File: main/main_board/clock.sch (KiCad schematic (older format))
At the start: 12 parts, among them U10 74AUP1G74, U11 MCP1755S-3302E/DB, U12 FIN1047, X1 Si570

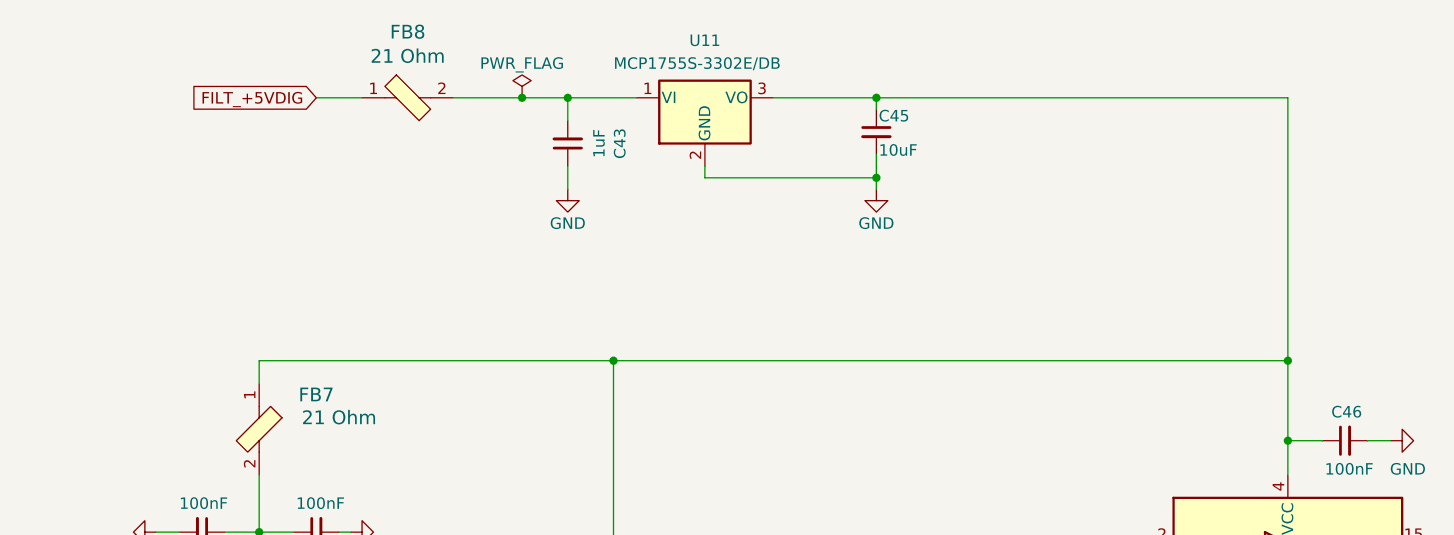
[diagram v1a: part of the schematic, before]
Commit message: A bunch of thinking about RFI and ESD, and some testing.  Mostly reflected in notebook.txt. Also another more explicit round of consideration of box-level grounding and power distribution, because this affects the power conditioning on the main board.  Power nets on the main board are mostly captured.  I added supply decoupling at each plugin slot.
in_filter.sxsch: added simulation of ESD, use vendor models for TVS diode and ferrite.

power_budget.xlsx: get rid of sheets for the input boards not implemented.  Add sheet for
the main board and carry over data from the input board sheet.
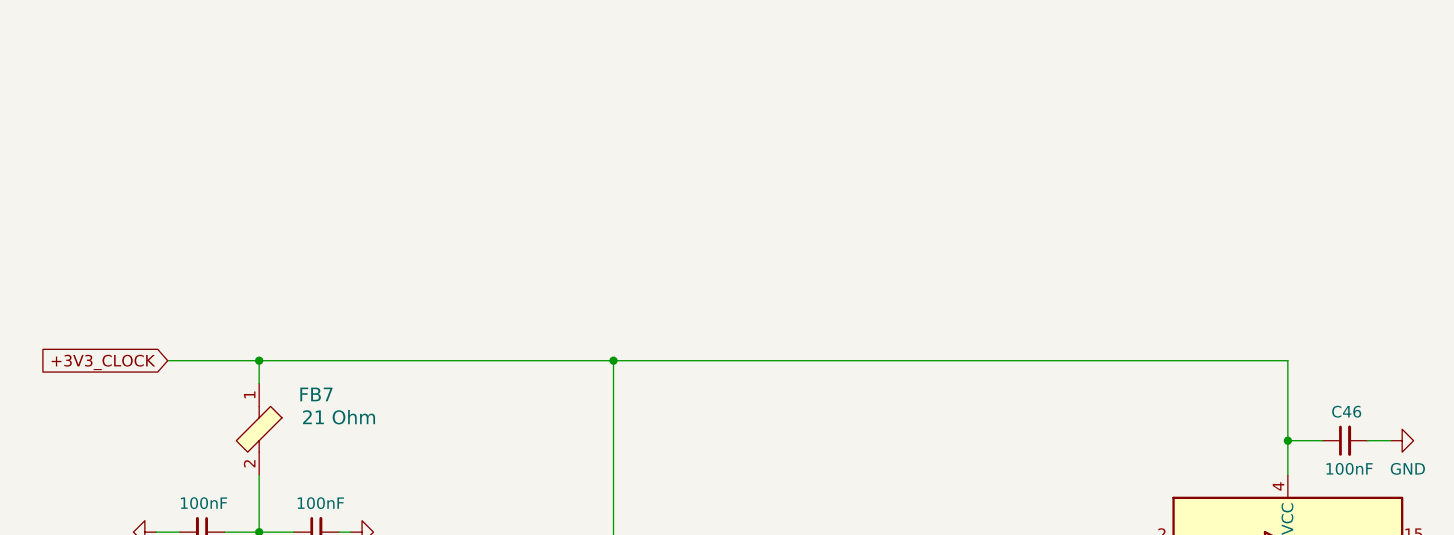
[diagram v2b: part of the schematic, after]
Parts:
- removed C43: 1uF, Capacitor_SMD:C_0805_2012Metric, symbol Device:C_Small
- removed C45: 10uF, Capacitor_SMD:C_0603_1608Metric, symbol Device:C_Small
- removed FB8: 21 Ohm, Inductor_SMD:L_0805_2012Metric, symbol dk_Ferrite-Beads-and-Chips:MPZ2012S601AT000
- removed U11: MCP1755S-3302E/DB, Package_TO_SOT_SMD:SOT-223-3_TabPin2, symbol Regulator_Linear:MCP1703A-1202_SOT223
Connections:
- net labels added: +3V3_CLOCK
- net labels removed: FILT_+5VDIG
- wire segments 64 -> 51
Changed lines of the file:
@@
 	4500 5100 4500 5250
 Connection ~ 4500 5250
-Text GLabel 3200 2150 0    50   Input ~ 0
-FILT_+5VDIG
-$Comp
-L Regulator_Linear:MCP1703A-1202_SOT223 U?
-U 1 1 5EC36C64
-P 4900 2150
-AR Path="/5E624B3C/5E51E83D/5EC36C64" Ref="U?"  Part="1"
-AR Path="/5E525F2C/5EC36C64" Ref="U11"  Part="1"
-F 0 "U11" H 4900 2400 50  0000 C CNN
-F 1 "MCP1755S-3302E/DB" H 4500 2300 50  0000 L CNN
-F 2 "Package_TO_SOT_SMD:SOT-223-3_TabPin2" H 4900 2350 50  0001 C CNN
-F 3 "http://www.microchip.com/mymicrochip/filehandler.aspx?ddocname=en560605" H 4900 2100 50  0001 C CNN
-F 4 "MCP1755S-3302E/DB-ND" H 4900 2150 50  0001 C CNN "Digikey"
-F 5 "IC REG LIN 3.3V 300MA SOT223-3" H 4900 2150 50  0001 C CNN "Description"
-F 6 "25" H 4900 2150 50  0001 C CNN "DK line"
-	1    4900 2150
-	1    0    0    -1
-$EndComp
-$Comp
-L dk_Ferrite-Beads-and-Chips:MPZ2012S601AT000 FB?
-U 1 1 5EC36C6F
-P 3600 2150
-AR Path="/5DFCF14D/5DE42731/5EC36C6F" Ref="FB?"  Part="1"
-AR Path="/5DFCF14D/5EC36C6F" Ref="FB?"  Part="1"
-AR Path="/5DFCF14D/5DA78AA2/5EC36C6F" Ref="FB?"  Part="1"
-AR Path="/5E51E83D/5EC36C6F" Ref="FB?"  Part="1"
-AR Path="/5E624B3C/5E51E83D/5EC36C6F" Ref="FB?"  Part="1"
-AR Path="/5E525F2C/5EC36C6F" Ref="FB8"  Part="1"
-F 0 "FB8" H 3600 2437 60  0000 C CNN
-F 1 "21 Ohm" H 3600 2331 60  0000 C CNN
-F 2 "Inductor_SMD:L_0805_2012Metric" H 3800 2350 60  0001 L CNN
-F 3 "https://www.yuden.co.jp/productdata/catalog/chipbeads01_e.pdf" H 3800 2450 60  0001 L CNN
-F 4 "HZ0805C202R-10" H 3800 2650 60  0001 L CNN "MPN"
-F 5 "Ferrite Beads and Chips" H 3800 2850 60  0001 L CNN "Family"
-F 6 "FERRITE BEAD 21 OHM 0805, 100 nH, 5 mOhm" H 3800 3150 60  0001 L CNN "Description"
-F 7 "587-1765-1-ND" H 3600 2150 50  0001 C CNN "Digikey"
-F 8 "24" H 3600 2150 50  0001 C CNN "DK line"
-	1    3600 2150
-	1    0    0    -1
-$EndComp
-$Comp
-L Device:C_Small C?
-U 1 1 5EC36C79
-P 4300 2350
-AR Path="/5DFF6C0D/5EC36C79" Ref="C?"  Part="1"
-AR Path="/5E1D6729/5E1DA2AA/5EC36C79" Ref="C?"  Part="1"
-AR Path="/5E2EB92B/5EC36C79" Ref="C?"  Part="1"
-AR Path="/5E51E83D/5EC36C79" Ref="C?"  Part="1"
-AR Path="/5E624B3C/5E51E83D/5EC36C79" Ref="C?"  Part="1"
-AR Path="/5E525F2C/5EC36C79" Ref="C43"  Part="1"
-F 0 "C43" V 4071 2350 50  0000 C CNN
-F 1 "1uF" V 4162 2350 50  0000 C CNN
-F 2 "Capacitor_SMD:C_0805_2012Metric" H 4300 2350 50  0001 C CNN
-F 3 "https://media.digikey.com/pdf/Data%20Sheets/Samsung%20PDFs/CL_Series_MLCC_ds.pdf" H 4300 2350 50  0001 C CNN
-F 4 "CAP CER 1UF 16V X7R 0805 " H 4300 2350 50  0001 C CNN "Description"
-F 5 "1276-6471-1-ND" H 4300 2350 50  0001 C CNN "Digikey"
-F 6 "CL21B105KOFNNNG" H 4300 2350 50  0001 C CNN "MPN"
-F 7 "27" H 4300 2350 50  0001 C CNN "DK line"
-	1    4300 2350
-	-1   0    0    1
-$EndComp
-Wire Wire Line
-	4300 2250 4300 2150
-Connection ~ 4300 2150
-Wire Wire Line
-	4300 2150 4600 2150
-Wire Wire Line
-	4300 2450 4300 2550
-Wire Wire Line
-	5650 2150 5650 2200
-Connection ~ 5650 2150
-Wire Wire Line
-	5650 2150 5200 2150
-Wire Wire Line
-	5650 2400 5650 2500
-Wire Wire Line
-	5650 2500 4900 2500
-Connection ~ 5650 2500
-Wire Wire Line
-	5650 2500 5650 2550
-Wire Wire Line
-	4900 2500 4900 2450
-Wire Wire Line
-	3200 2150 3400 2150
-$Comp
-L power:PWR_FLAG #FLG?
-U 1 1 5EC36CA7
-P 4100 2150
-AR Path="/5E624B3C/5E51E83D/5EC36CA7" Ref="#FLG?"  Part="1"
-AR Path="/5E525F2C/5EC36CA7" Ref="#FLG01"  Part="1"
-F 0 "#FLG01" H 4100 2225 50  0001 C CNN
-F 1 "PWR_FLAG" H 4100 2300 50  0000 C CNN
-F 2 "" H 4100 2150 50  0001 C CNN
-F 3 "~" H 4100 2150 50  0001 C CNN
-	1    4100 2150
-	1    0    0    -1
-$EndComp
-Connection ~ 4100 2150
-Wire Wire Line
-	4100 2150 4300 2150
-$Comp
-L power:GND #PWR?
-U 1 1 5EC36CB5
-P 5650 2550
-AR Path="/5E624B3C/5E51E83D/5EC36CB5" Ref="#PWR?"  Part="1"
-AR Path="/5E525F2C/5EC36CB5" Ref="#PWR051"  Part="1"
-F 0 "#PWR051" H 5650 2300 50  0001 C CNN
-F 1 "GND" H 5650 2400 50  0000 C CNN
-F 2 "" H 5650 2550 50  0001 C CNN
-F 3 "" H 5650 2550 50  0001 C CNN
-	1    5650 2550
-	1    0    0    -1
-$EndComp
-$Comp
-L power:GND #PWR?
-U 1 1 5EC36CBB
-P 4300 2550
-AR Path="/5E624B3C/5E51E83D/5EC36CBB" Ref="#PWR?"  Part="1"
-AR Path="/5E525F2C/5EC36CBB" Ref="#PWR048"  Part="1"
-F 0 "#PWR048" H 4300 2300 50  0001 C CNN
-F 1 "GND" H 4300 2400 50  0000 C CNN
-F 2 "" H 4300 2550 50  0001 C CNN
-F 3 "" H 4300 2550 50  0001 C CNN
-	1    4300 2550
-	1    0    0    -1
-$EndComp
-Wire Wire Line
-	3800 2150 4100 2150
-$Comp
-L Device:C_Small C?
-U 1 1 5EC40A92
-P 5650 2300
-AR Path="/5DFCF14D/5DA78AA2/5EC40A92" Ref="C?"  Part="1"
-AR Path="/5DFCF14D/5E295469/5EC40A92" Ref="C?"  Part="1"
-AR Path="/5E448095/5DA78AA2/5EC40A92" Ref="C?"  Part="1"
-AR Path="/5E45936E/5DA78AA2/5EC40A92" Ref="C?"  Part="1"
-AR Path="/5E525F2C/5E6427A0/5DA78AA2/5EC40A92" Ref="C?"  Part="1"
-AR Path="/5E624B3C/5DFCF14D/5DA78AA2/5EC40A92" Ref="C?"  Part="1"
-AR Path="/5E624B3C/5E448095/5DA78AA2/5EC40A92" Ref="C?"  Part="1"
-AR Path="/5E624B3C/5E45936E/5DA78AA2/5EC40A92" Ref="C?"  Part="1"
-AR Path="/5E525F2C/5EC40A92" Ref="C45"  Part="1"
-F 0 "C45" H 5660 2370 50  0000 L CNN
-F 1 "10uF" H 5660 2220 50  0000 L CNN
-F 2 "Capacitor_SMD:C_0603_1608Metric" H 5650 2300 50  0001 C CNN
-F 3 "http://datasheets.avx.com/cx5r.pdf" H 5650 2300 50  0001 C CNN
-F 4 "CAP CER 10UF 6.3V X5R 0603" H 5650 2300 50  0001 C CNN "Description"
-F 5 "478-5318-1-ND" H 5650 2300 50  0001 C CNN "Digikey"
-F 6 "06036D106MAT2A" H 5650 2300 50  0001 C CNN "MPN"
-F 7 "29" H 5650 2300 50  0001 C CNN "DK line"
-	1    5650 2300
-	1    0    0    -1
-$EndComp
+Text GLabel 2550 3300 0    50   Input ~ 0
++3V3_CLOCK
 $Comp
 L dk_Ferrite-Beads-and-Chips:MPZ2012S601AT000 FB?
@@
 $EndComp
 Wire Wire Line
-	7450 2150 7450 3300
-Wire Wire Line
 	7450 3300 4500 3300
 Wire Wire Line
 	2950 3300 2950 3400
-Wire Wire Line
-	5650 2150 7450 2150
 Wire Wire Line
 	4500 3300 4500 5100
@@
 Wire Wire Line
 	7450 3300 7450 3650
-Connection ~ 7450 3300
 Text Notes 8800 4800 0    50   ~ 0
 To FPGA
@@
 Wire Wire Line
 	4350 5250 4500 5250
+Wire Wire Line
+	2550 3300 2950 3300
+Connection ~ 2950 3300
 $EndSCHEMATC

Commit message: Mostly work on hooking in the Microzed using kipart symbols and a footprint. Also added 2.5V VCCIO regulator.
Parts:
- added J2: MCLK, Connector_Coaxial:MMCX_Molex_73415-1471_Vertical, symbol Connector:Conn_Coaxial
- added R7: 1K, Resistor_SMD:R_0603_1608Metric, symbol Device:R_US
- added R8: 33, Resistor_SMD:R_0603_1608Metric, symbol Device:R_US
- renumbered X1 to X2
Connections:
- net labels added: FPGA_SYSCLK+, FPGA_SYSCLK-, MCLK_JACK, OUT_SYSCLK+, OUT_SYSCLK-
- net labels removed: FPGA_CLK+, FPGA_CLK-, OUT_CLK+, OUT_CLK-
- wire segments 51 -> 57
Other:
- moved on the sheet: C41, C42, C44, C46, FB7, U10, U12, X2

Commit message: Schematic is mostly complete (except for BIST DACs), and passes ERC.  Rough placement of components on PCB.
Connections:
- wire segments 57 -> 59
- no-connect marks 0 -> 8
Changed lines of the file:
@@
 $EndComp
 Wire Wire Line
-	2900 2700 2900 2950
+	2900 2700 2900 2750
 $Comp
 L Device:C_Small C?
@@
 AR Path="/5E525FFE/5EBFB7CD" Ref="U?"  Part="1"
 F 0 "U12" H 7450 2750 50  0000 L CNN
-F 1 "FIN1047" H 7600 2750 50  0000 L CNN
+F 1 "FIN1047" H 7450 2650 50  0000 L CNN
 F 2 "Package_SO:TSSOP-16_4.4x5mm_P0.65mm" H 7300 2650 50  0001 C CNN
 F 3 "https://www.onsemi.com/pub/Collateral/FIN1047-D.pdf" H 7450 3600 50  0001 C CNN
@@
 Wire Wire Line
 	5600 5000 5600 5150
+$Comp
+L power:PWR_FLAG #FLG?
+U 1 1 5EE734B2
+P 3550 2750
+AR Path="/5E624B3C/5E51E83D/5EE734B2" Ref="#FLG?"  Part="1"
+AR Path="/5E525F2C/5EE734B2" Ref="#FLG0103"  Part="1"
+AR Path="/5E525FC9/5EE734B2" Ref="#FLG?"  Part="1"
+F 0 "#FLG0103" H 3550 2825 50  0001 C CNN
+F 1 "PWR_FLAG" H 3550 2900 50  0000 C CNN
+F 2 "" H 3550 2750 50  0001 C CNN
+F 3 "~" H 3550 2750 50  0001 C CNN
+	1    3550 2750
+	0    1    1    0
+$EndComp
+Wire Wire Line
+	3550 2750 2900 2750
+Connection ~ 2900 2750
+Wire Wire Line
+	2900 2750 2900 2950
+NoConn ~ 3350 3900
+NoConn ~ 4700 4550
+NoConn ~ 8000 3400
+NoConn ~ 8000 3300
+NoConn ~ 8000 3100
+NoConn ~ 8000 3000
+NoConn ~ 6750 3000
+NoConn ~ 6750 3300
 $EndSCHEMATC

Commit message: Mostly work on main board layout. Aligned things on mm grid for easier routing, moved things around to create routing area. Neatened up component groups onto the grid. Parts of the routing plan are now drawn on the PCB.  See also notebook.txt. Reduced pad size of the PCIE connector, tweaked design rule clearances. Minor schematic tweaks.
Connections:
- net labels added: CLK_DIST, MCLK_DIST, VDD_CLK
- net labels removed: OVDD
- wire segments 59 -> 61
- no-connect marks 8 -> 6
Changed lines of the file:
@@
 	7400 4550 7400 4600
-$Comp
-L ilemt_input:OVDD #PWR052
-U 1 1 5EBFB7C3
-P 6650 4200
-AR Path="/5E525F2C/5EBFB7C3" Ref="#PWR052"  Part="1"
-AR Path="/5E525FFE/5EBFB7C3" Ref="#PWR?"  Part="1"
-F 0 "#PWR052" H 6650 4050 50  0001 C CNN
-F 1 "OVDD" H 6650 4350 50  0000 C CNN
-F 2 "" H 6650 4200 50  0001 C CNN
-F 3 "" H 6650 4200 50  0001 C CNN
-	1    6650 4200
-	1    0    0    -1
-$EndComp
-Wire Wire Line
-	6650 4200 6800 4200
 $Comp
 L Interface:SN65LVDS047PW U12
@@
 $EndComp
 Wire Wire Line
-	7400 2200 4450 2200
+	7400 2200 6350 2200
 Wire Wire Line
 	2900 2200 2900 2300
@@
 NoConn ~ 8000 3100
 NoConn ~ 8000 3000
-NoConn ~ 6750 3000
-NoConn ~ 6750 3300
+Text Label 2500 3250 0    50   ~ 0
+VDD_CLK
+Text Label 4800 3600 0    50   ~ 0
+CLK_DIST
+Text Label 5200 4350 0    50   ~ 0
+MCLK_DIST
+Wire Wire Line
+	6350 4200 6350 2200
+Wire Wire Line
+	6350 4200 6800 4200
+Connection ~ 6350 2200
+Wire Wire Line
+	6350 2200 4450 2200
 $EndSCHEMATC
